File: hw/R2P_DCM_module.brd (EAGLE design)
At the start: 40 x 60 mm, 53 parts, among them U1 STM32F103CX, U5 LD3985XX, X1 MICROMATCH-4, X2 OSC-XTAL212M_

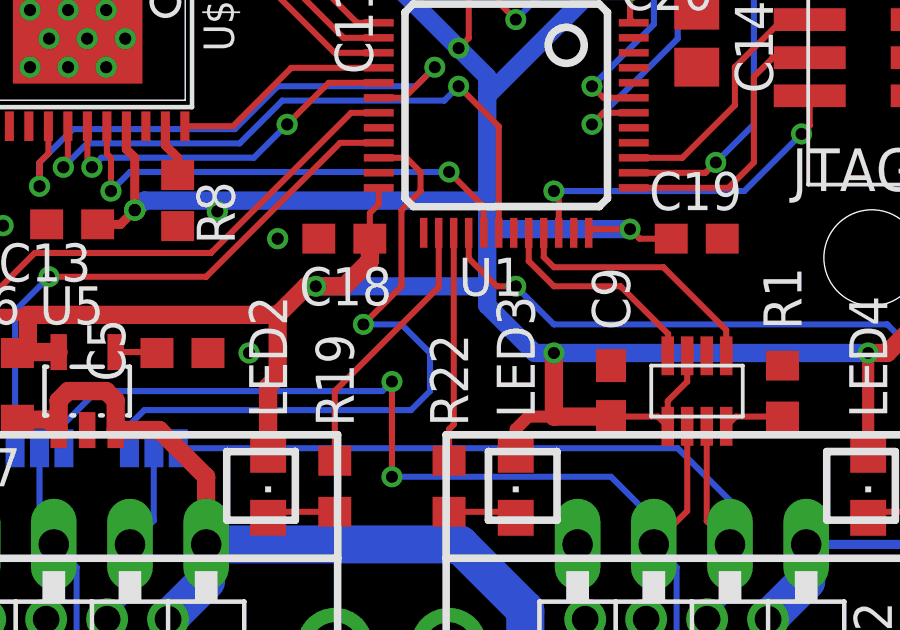
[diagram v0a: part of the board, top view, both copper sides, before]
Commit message: Removed misplaced via and disconnected MAX3051 shutdown pin
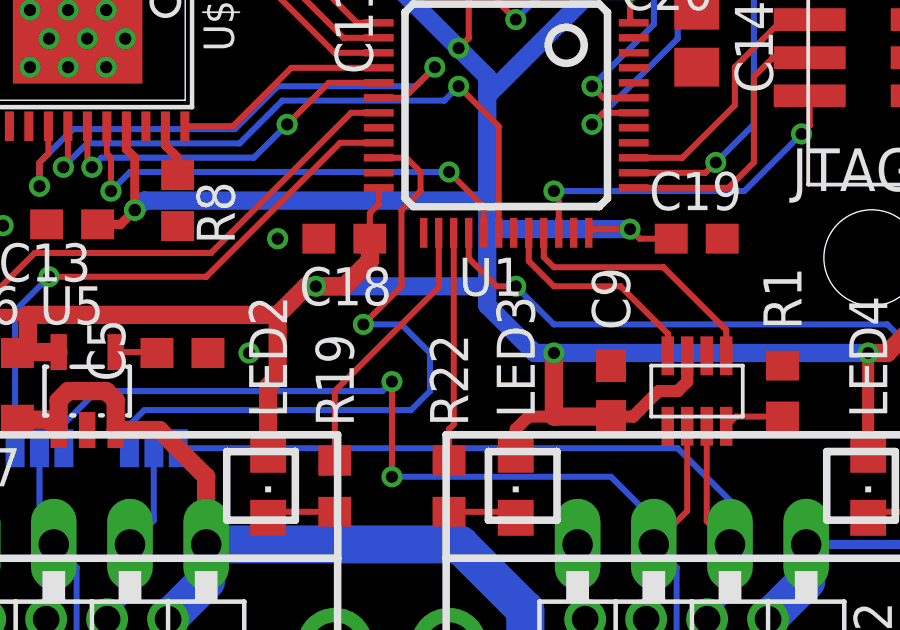
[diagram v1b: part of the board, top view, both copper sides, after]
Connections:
- net +3V3: no longer SOT1.P$5
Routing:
- net +3V3: track 140.8 -> 140.0 mm
- net GND: vias 49 -> 48
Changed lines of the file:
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@@
 <layer number="23" name="tOrigins" color="15" fill="1" visible="yes" active="yes"/>
 <layer number="24" name="bOrigins" color="15" fill="1" visible="no" active="yes"/>
-<layer number="25" name="tNames" color="7" fill="1" visible="yes" active="yes"/>
+<layer number="25" name="tNames" color="7" fill="1" visible="no" active="yes"/>
 <layer number="26" name="bNames" color="7" fill="1" visible="no" active="yes"/>
 <layer number="27" name="tValues" color="7" fill="1" visible="no" active="yes"/>
 <layer number="28" name="bValues" color="7" fill="1" visible="no" active="yes"/>
-<layer number="29" name="tStop" color="7" fill="3" visible="yes" active="yes"/>
+<layer number="29" name="tStop" color="7" fill="3" visible="no" active="yes"/>
 <layer number="30" name="bStop" color="7" fill="6" visible="no" active="yes"/>
 <layer number="31" name="tCream" color="7" fill="4" visible="no" active="yes"/>
@@
 <layer number="33" name="tFinish" color="6" fill="3" visible="no" active="yes"/>
 <layer number="34" name="bFinish" color="6" fill="6" visible="no" active="yes"/>
-<layer number="35" name="tGlue" color="7" fill="4" visible="yes" active="yes"/>
+<layer number="35" name="tGlue" color="7" fill="4" visible="no" active="yes"/>
 <layer number="36" name="bGlue" color="7" fill="5" visible="no" active="yes"/>
 <layer number="37" name="tTest" color="7" fill="1" visible="yes" active="yes"/>
@@
 <layer number="41" name="tRestrict" color="4" fill="10" visible="yes" active="yes"/>
 <layer number="42" name="bRestrict" color="1" fill="10" visible="no" active="yes"/>
-<layer number="43" name="vRestrict" color="2" fill="10" visible="no" active="yes"/>
+<layer number="43" name="vRestrict" color="2" fill="10" visible="yes" active="yes"/>
 <layer number="44" name="Drills" color="7" fill="1" visible="yes" active="yes"/>
 <layer number="45" name="Holes" color="7" fill="1" visible="yes" active="yes"/>
@@
 <layer number="47" name="Measures" color="7" fill="1" visible="yes" active="yes"/>
 <layer number="48" name="Document" color="7" fill="1" visible="yes" active="yes"/>
-<layer number="49" name="Reference" color="7" fill="1" visible="no" active="yes"/>
-<layer number="50" name="dxf" color="7" fill="1" visible="no" active="yes"/>
+<layer number="49" name="Reference" color="7" fill="1" visible="yes" active="yes"/>
+<layer number="50" name="dxf" color="7" fill="1" visible="yes" active="yes"/>
 <layer number="51" name="tDocu" color="7" fill="1" visible="yes" active="yes"/>
 <layer number="52" name="bDocu" color="7" fill="1" visible="no" active="yes"/>
@@
 <layer number="107" name="Crop" color="7" fill="1" visible="no" active="yes"/>
 <layer number="116" name="Patch_BOT" color="9" fill="4" visible="no" active="yes"/>
-<layer number="121" name="_tsilk" color="7" fill="1" visible="yes" active="yes"/>
+<layer number="121" name="_tsilk" color="7" fill="1" visible="no" active="yes"/>
 <layer number="122" name="_bsilk" color="7" fill="1" visible="no" active="yes"/>
 <layer number="125" name="_tNames" color="7" fill="1" visible="no" active="yes"/>
@@
 <contactref element="C13" pad="2"/>
 <via x="7.03875" y="20.43875" extent="1-16" drill="0.4064" shape="octagon"/>
-<via x="14.1825" y="20.915" extent="1-16" drill="0.4064" shape="octagon"/>
 <contactref element="U$1" pad="PAD"/>
 <via x="7.9375" y="27.6225" extent="1-16" drill="0.4064" shape="octagon"/>
@@
 <contactref element="U$4" pad="P$1"/>
 <contactref element="SOT1" pad="P$3"/>
-<contactref element="SOT1" pad="P$5"/>
 <contactref element="U5" pad="5"/>
 <contactref element="C6" pad="1"/>
@@
 <wire x1="27.94" y1="20.32" x2="26.685" y2="20.32" width="0.2032" layer="1"/>
 <wire x1="26.685" y1="20.32" x2="26.5625" y2="20.1975" width="0.2032" layer="1"/>
-<wire x1="27.305" y1="14.0725" x2="28.87" y2="14.0725" width="0.2032" layer="1"/>
-<wire x1="28.87" y1="14.0725" x2="29.195" y2="13.7475" width="0.2032" layer="1"/>
 <wire x1="25.4" y1="14.0725" x2="24.55" y2="14.0725" width="0.4064" layer="1"/>
 <wire x1="25.4" y1="14.0725" x2="27.305" y2="14.0725" width="0.6096" layer="1"/>
 <wire x1="24.55" y1="14.0725" x2="24.13" y2="13.6525" width="0.4064" layer="1"/>
 <wire x1="24.13" y1="13.6525" x2="24.13" y2="12.7975" width="0.4064" layer="1"/>
-<wire x1="29.195" y1="13.7475" x2="29.195" y2="14.59" width="0.2032" layer="1"/>
-<wire x1="29.195" y1="14.59" x2="29.845" y2="15.24" width="0.2032" layer="1"/>
-<wire x1="29.845" y1="15.24" x2="29.845" y2="16.0975" width="0.2032" layer="1"/>
 <wire x1="27.94" y1="27.32" x2="28.0625" y2="27.1975" width="0.2032" layer="1"/>
 <wire x1="27.94" y1="28.2575" x2="27.94" y2="27.32" width="0.2032" layer="1"/>
@@
 <wire x1="10.1925" y1="20.47875" x2="10.95355" y2="20.47875" width="0.3048" layer="1"/>
 <wire x1="10.95355" y1="20.47875" x2="11.43" y2="20.9552" width="0.3048" layer="1"/>
+<wire x1="29.845" y1="16.0975" x2="29.845" y2="15.24" width="0.4064" layer="1"/>
+<wire x1="29.845" y1="15.24" x2="29.5275" y2="14.9225" width="0.4064" layer="1"/>
+<wire x1="29.5275" y1="14.9225" x2="28.8925" y2="14.9225" width="0.4064" layer="1"/>
+<wire x1="28.8925" y1="14.9225" x2="28.2575" y2="14.2875" width="0.4064" layer="1"/>
+<wire x1="27.305" y1="14.0725" x2="28.0425" y2="14.0725" width="0.4064" layer="1"/>
+<wire x1="28.0425" y1="14.0725" x2="28.2575" y2="14.2875" width="0.4064" layer="1"/>
 </signal>
 <signal name="JTMS">

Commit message: increased bootstrap capacitor value
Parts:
- C1, C3: value 100n -> 220n
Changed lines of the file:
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@@
 <?xml version="1.0" encoding="utf-8"?>
 <!DOCTYPE eagle SYSTEM "eagle.dtd">
-<eagle version="6.2">
+<eagle version="6.4">
 <drawing>
 <settings>
@@
 <hole x="36" y="19.365" drill="3.2"/>
 <hole x="4" y="56" drill="3.2"/>
-<dimension x1="0" y1="0" x2="0" y2="60" x3="-4" y3="30" layer="16"/>
-<dimension x1="40" y1="60" x2="0" y2="60" x3="20" y3="63.5" layer="16"/>
+<dimension x1="0" y1="0" x2="0" y2="60" x3="-4" y3="30" textsize="3.5" layer="16"/>
+<dimension x1="40" y1="60" x2="0" y2="60" x3="20" y3="63.5" textsize="3.5" layer="16"/>
 </plain>
 <attributes>
@@
 </class>
 </classes>
-<designrules>
+<designrules name="default">
 <description language="de">&lt;b&gt;EAGLE Design Rules&lt;/b&gt;
 &lt;p&gt;
@@
 <element name="R4" library="rcl" package="R0603" value="10" x="10.3188" y="34.6075" rot="R90"/>
 <element name="R5" library="rcl" package="R0603" value="10" x="12.5413" y="34.6075" rot="R90"/>
-<element name="C1" library="rcl" package="C0603" value="100n" x="7.6199" y="32.0675" rot="R180"/>
-<element name="C3" library="rcl" package="C0603" value="100n" x="10.795" y="32.0675"/>
+<element name="C1" library="rcl" package="C0603" value="220n" x="7.6199" y="32.0675" rot="R180"/>
+<element name="C3" library="rcl" package="C0603" value="220n" x="10.795" y="32.0675"/>
 <element name="U$2" library="SparkFun" package="SO08" value="ACS712" x="20.0025" y="40.9575" rot="R180"/>
 <element name="C10" library="rcl" package="C0603" value="100n" x="24.4475" y="36.5125"/>

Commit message: Corrected RDEAD value
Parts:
- R8: value 10 -> 10k
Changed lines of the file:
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@@
 <element name="C2" library="rcl" package="C0805" value="" x="14.9224" y="31.75" rot="R270"/>
 <element name="C4" library="rcl" package="C0603" value="470n" x="4.39625" y="24.83" rot="R270"/>
-<element name="R8" library="rcl" package="R0603" value="10" x="12.8587" y="21.2727" rot="R270"/>
+<element name="R8" library="rcl" package="R0603" value="10k" x="12.8587" y="21.2727" rot="R270"/>
 <element name="C13" library="rcl" package="C0603" value="100n" x="9.3425" y="20.47875" rot="R180"/>
 </elements>

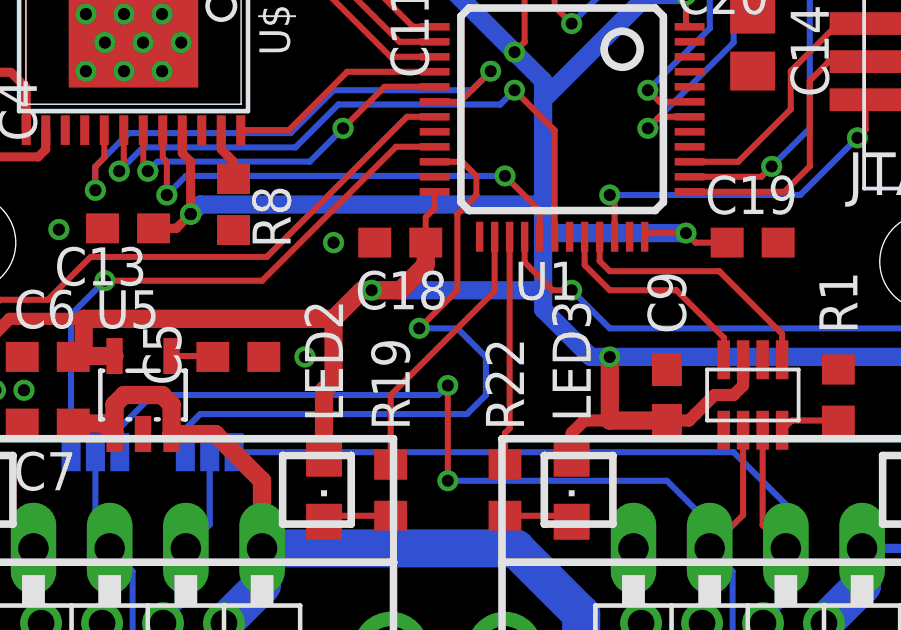
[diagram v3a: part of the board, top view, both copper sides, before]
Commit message: removed duplicated via
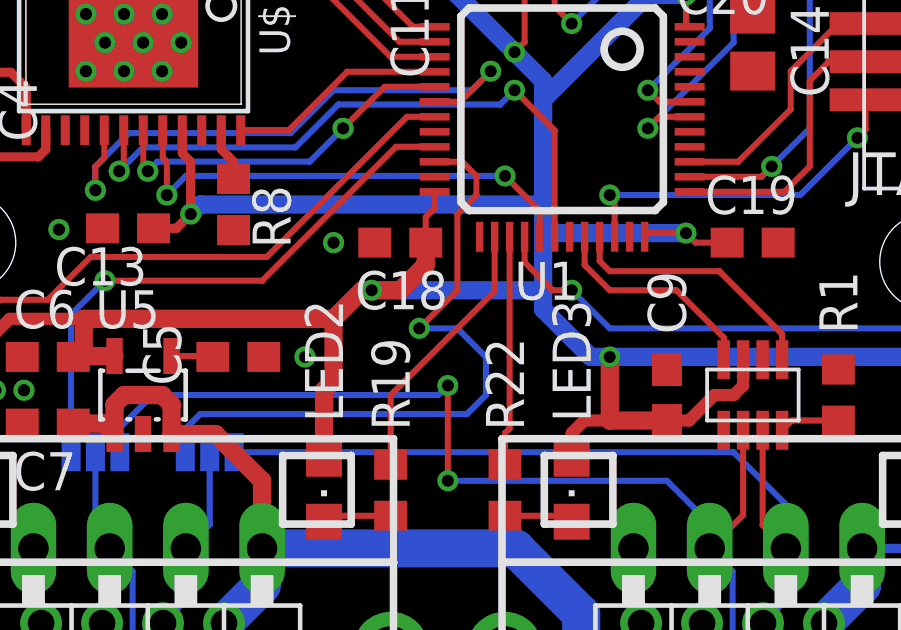
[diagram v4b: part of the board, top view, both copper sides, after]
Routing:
- net +3V3: vias 9 -> 8
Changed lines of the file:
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@@
 <grid distance="0.0125" unitdist="inch" unit="inch" style="lines" multiple="1" display="no" altdistance="0.00625" altunitdist="inch" altunit="inch"/>
 <layers>
-<layer number="1" name="Top" color="4" fill="1" visible="yes" active="yes"/>
+<layer number="1" name="Top" color="4" fill="1" visible="no" active="yes"/>
 <layer number="2" name="Route2" color="1" fill="3" visible="no" active="yes"/>
 <layer number="3" name="Route3" color="4" fill="3" visible="no" active="yes"/>
@@
 <layer number="14" name="Route14" color="1" fill="6" visible="no" active="yes"/>
 <layer number="15" name="Route15" color="4" fill="6" visible="no" active="yes"/>
-<layer number="16" name="Bottom" color="1" fill="1" visible="no" active="yes"/>
+<layer number="16" name="Bottom" color="1" fill="1" visible="yes" active="yes"/>
 <layer number="17" name="Pads" color="2" fill="1" visible="yes" active="yes"/>
 <layer number="18" name="Vias" color="2" fill="1" visible="yes" active="yes"/>
 <layer number="19" name="Unrouted" color="6" fill="1" visible="yes" active="yes"/>
 <layer number="20" name="Dimension" color="15" fill="1" visible="yes" active="yes"/>
-<layer number="21" name="tPlace" color="7" fill="1" visible="yes" active="yes"/>
-<layer number="22" name="bPlace" color="7" fill="1" visible="no" active="yes"/>
-<layer number="23" name="tOrigins" color="15" fill="1" visible="yes" active="yes"/>
-<layer number="24" name="bOrigins" color="15" fill="1" visible="no" active="yes"/>
+<layer number="21" name="tPlace" color="7" fill="1" visible="no" active="yes"/>
+<layer number="22" name="bPlace" color="7" fill="1" visible="yes" active="yes"/>
+<layer number="23" name="tOrigins" color="15" fill="1" visible="no" active="yes"/>
+<layer number="24" name="bOrigins" color="15" fill="1" visible="yes" active="yes"/>
 <layer number="25" name="tNames" color="7" fill="1" visible="no" active="yes"/>
 <layer number="26" name="bNames" color="7" fill="1" visible="no" active="yes"/>
@@
 <layer number="35" name="tGlue" color="7" fill="4" visible="no" active="yes"/>
 <layer number="36" name="bGlue" color="7" fill="5" visible="no" active="yes"/>
-<layer number="37" name="tTest" color="7" fill="1" visible="yes" active="yes"/>
+<layer number="37" name="tTest" color="7" fill="1" visible="no" active="yes"/>
 <layer number="38" name="bTest" color="7" fill="1" visible="no" active="yes"/>
-<layer number="39" name="tKeepout" color="4" fill="11" visible="yes" active="yes"/>
-<layer number="40" name="bKeepout" color="1" fill="11" visible="no" active="yes"/>
-<layer number="41" name="tRestrict" color="4" fill="10" visible="yes" active="yes"/>
-<layer number="42" name="bRestrict" color="1" fill="10" visible="no" active="yes"/>
-<layer number="43" name="vRestrict" color="2" fill="10" visible="yes" active="yes"/>
+<layer number="39" name="tKeepout" color="4" fill="11" visible="no" active="yes"/>
+<layer number="40" name="bKeepout" color="1" fill="11" visible="yes" active="yes"/>
+<layer number="41" name="tRestrict" color="4" fill="10" visible="no" active="yes"/>
+<layer number="42" name="bRestrict" color="1" fill="10" visible="yes" active="yes"/>
+<layer number="43" name="vRestrict" color="2" fill="10" visible="no" active="yes"/>
 <layer number="44" name="Drills" color="7" fill="1" visible="yes" active="yes"/>
-<layer number="45" name="Holes" color="7" fill="1" visible="yes" active="yes"/>
-<layer number="46" name="Milling" color="3" fill="1" visible="yes" active="yes"/>
-<layer number="47" name="Measures" color="7" fill="1" visible="yes" active="yes"/>
-<layer number="48" name="Document" color="7" fill="1" visible="yes" active="yes"/>
-<layer number="49" name="Reference" color="7" fill="1" visible="yes" active="yes"/>
-<layer number="50" name="dxf" color="7" fill="1" visible="yes" active="yes"/>
-<layer number="51" name="tDocu" color="7" fill="1" visible="yes" active="yes"/>
-<layer number="52" name="bDocu" color="7" fill="1" visible="no" active="yes"/>
+<layer number="45" name="Holes" color="7" fill="1" visible="no" active="yes"/>
+<layer number="46" name="Milling" color="3" fill="1" visible="no" active="yes"/>
+<layer number="47" name="Measures" color="7" fill="1" visible="no" active="yes"/>
+<layer number="48" name="Document" color="7" fill="1" visible="no" active="yes"/>
+<layer number="49" name="Reference" color="7" fill="1" visible="no" active="yes"/>
+<layer number="50" name="dxf" color="7" fill="1" visible="no" active="yes"/>
+<layer number="51" name="tDocu" color="7" fill="1" visible="no" active="yes"/>
+<layer number="52" name="bDocu" color="7" fill="1" visible="yes" active="yes"/>
 <layer number="53" name="tGND_GNDA" color="7" fill="9" visible="no" active="no"/>
 <layer number="54" name="bGND_GNDA" color="1" fill="9" visible="no" active="no"/>
@@
 <hole x="36" y="19.365" drill="3.2"/>
 <hole x="4" y="56" drill="3.2"/>
-<dimension x1="0" y1="0" x2="0" y2="60" x3="-4" y3="30" textsize="3.5" layer="16"/>
-<dimension x1="40" y1="60" x2="0" y2="60" x3="20" y3="63.5" textsize="3.5" layer="16"/>
 </plain>
 <attributes>
@@
 <via x="22.225" y="26.3525" extent="1-16" drill="0.4" shape="octagon"/>
 <via x="18.2562" y="33.8137" extent="1-16" drill="0.4" shape="octagon"/>
-<via x="11.4301" y="20.955" extent="1-16" drill="0.4064" shape="octagon"/>
 <via x="11.43" y="20.9552" extent="1-16" drill="0.4" shape="octagon"/>
 <contactref element="C13" pad="1"/>
@@
 <wire x1="29.845" y1="15.24" x2="29.5275" y2="14.9225" width="0.4064" layer="1"/>
 <wire x1="29.5275" y1="14.9225" x2="28.8925" y2="14.9225" width="0.4064" layer="1"/>
-<wire x1="28.8925" y1="14.9225" x2="28.2575" y2="14.2875" width="0.4064" layer="1"/>
+<wire x1="28.8925" y1="14.9225" x2="28.0425" y2="14.0725" width="0.4064" layer="1"/>
 <wire x1="27.305" y1="14.0725" x2="28.0425" y2="14.0725" width="0.4064" layer="1"/>
-<wire x1="28.0425" y1="14.0725" x2="28.2575" y2="14.2875" width="0.4064" layer="1"/>
 </signal>
 <signal name="JTMS">
@@
 <contactref element="U5" pad="4"/>
 <contactref element="C5" pad="1"/>
-<wire x1="12.1675" y1="16.1925" x2="12.1375" y2="16.2225" width="0.1524" layer="1"/>
+<wire x1="12.1675" y1="16.1925" x2="12.1375" y2="16.2225" width="0.2032" layer="1"/>
 <wire x1="10.7925" y1="16.2225" x2="12.1675" y2="16.2225" width="0.2032" layer="1"/>
 <wire x1="12.1675" y1="16.2225" x2="12.1675" y2="16.1925" width="0.2032" layer="1"/>
